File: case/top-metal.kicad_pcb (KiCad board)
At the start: 2 copper layers, 137.8 x 95.7 mm, 26 parts, among them SW1 SW_PUSH, SW10 SW_PUSH, SW11 SW_PUSH, SW12 SW_PUSH, SW13 SW_PUSH, SW14 SW_PUSH, SW15 SW_PUSH, SW16 SW_PUSH, SW17 SW_PUSH, SW18 SW_PUSH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

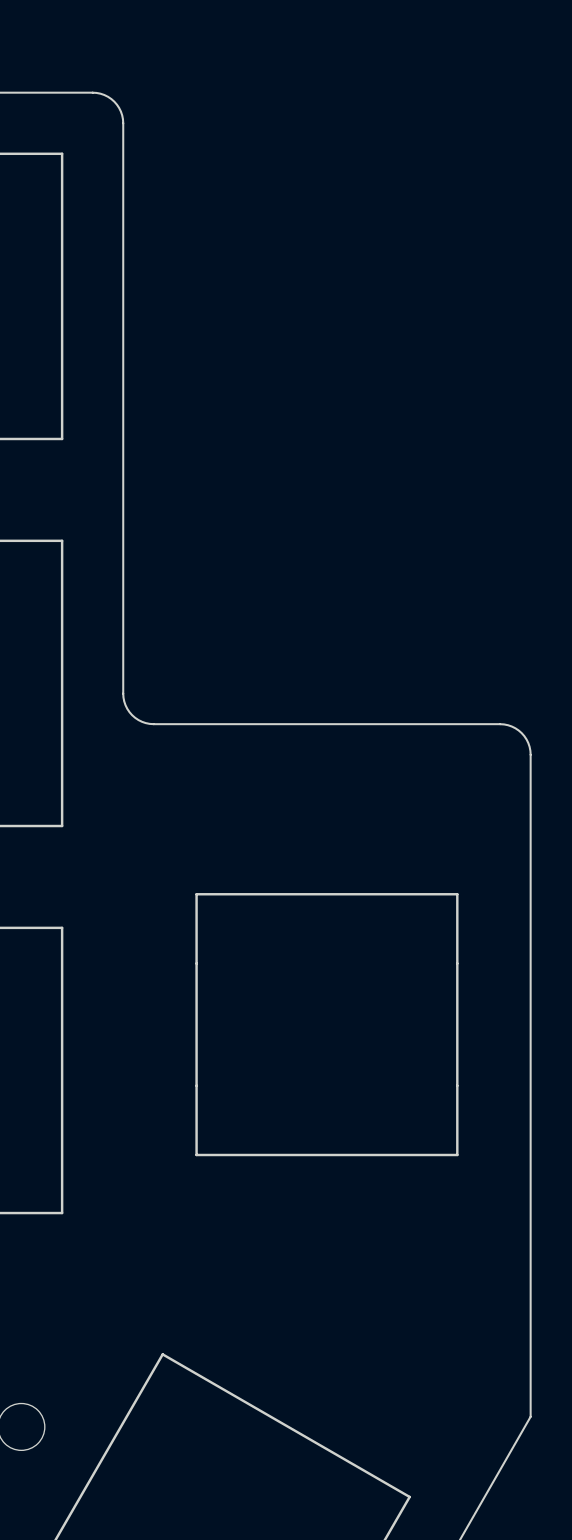
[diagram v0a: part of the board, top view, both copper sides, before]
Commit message: adjust top plate, add new cover in PCB style
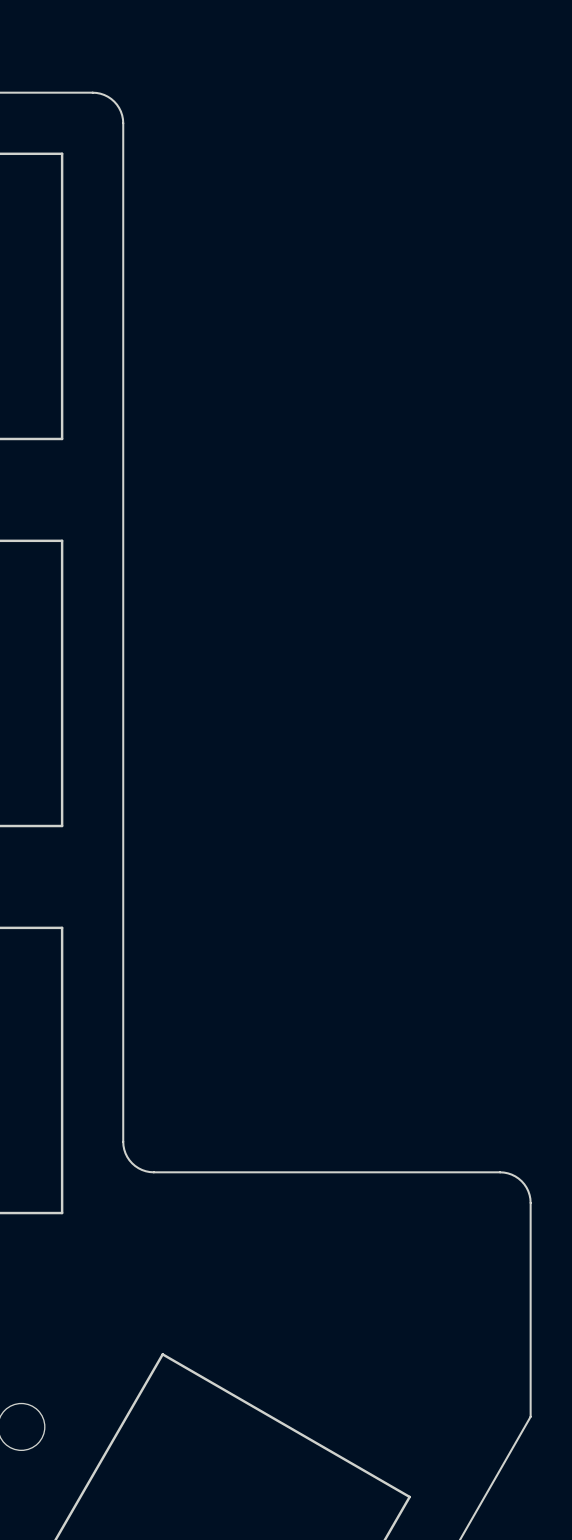
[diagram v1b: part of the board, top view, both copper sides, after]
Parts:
- removed RE1: RotaryEncoder_Switch, pica:EC11_Hole
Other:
- outline, holes or cut-outs redrawn
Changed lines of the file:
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@@
     (fp_line (start 9.525 -9.525) (end -9.525 -9.525) (layer "F.Fab") (width 0.15))
-  )
-  (footprint "pica:EC11_Hole" (layer "F.Cu")
-    (at 188.5 96.75)
-    (property "Sheetfile" "full.kicad_sch")
-    (property "Sheetname" "")
-    (attr through_hole)
-    (fp_text reference "RE1" (at 0 7.7 unlocked) (layer "F.SilkS") hide
-      (effects (font (size 1 1) (thickness 0.15)))
-    )
-    (fp_text value "RotaryEncoder_Switch" (at 0 -7.3 unlocked) (layer "F.Fab") hide
-      (effects (font (size 1 1) (thickness 0.15)))
-    )
-    (fp_line (start 6.4 6.4) (end -6.4 6.4) (layer "Edge.Cuts") (width 0.12))
-    (fp_line (start -6.4 -6.4) (end -6.4 -3) (layer "Edge.Cuts") (width 0.12))
-    (fp_line (start 6.4 -3) (end 6.4 3) (layer "Edge.Cuts") (width 0.12))
-    (fp_line (start 6.4 -3) (end 6.4 -6.4) (layer "Edge.Cuts") (width 0.12))
-    (fp_line (start -6.4 -6.4) (end 6.4 -6.4) (layer "Edge.Cuts") (width 0.12))
-    (fp_line (start -6.4 -3) (end -6.4 3) (layer "Edge.Cuts") (width 0.12))
-    (fp_line (start 6.4 6.4) (end 6.4 3) (layer "Edge.Cuts") (width 0.12))
-    (fp_line (start -6.4 3) (end -6.4 6.4) (layer "Edge.Cuts") (width 0.12))
   )
   (footprint "kbd:SW_Hole" (layer "F.Cu")
@@
   )
   (gr_line (start 103 48.5) (end 119 48.5) (layer "Edge.Cuts") (width 0.1))
-  (gr_line (start 180 82) (end 197 82) (layer "Edge.Cuts") (width 0.1))
+  (gr_arc (start 180 104) (mid 178.93934 103.56066) (end 178.5 102.5) (layer "Edge.Cuts") (width 0.1))
+  (gr_line (start 180 104) (end 197 104) (layer "Edge.Cuts") (width 0.1))
   (gr_arc (start 142 49) (mid 140.93934 48.56066) (end 140.5 47.5) (layer "Edge.Cuts") (width 0.1))
   (gr_arc (start 185.049038 139.450962) (mid 184.138233 140.149868) (end 183 140) (layer "Edge.Cuts") (width 0.1))
@@
   (gr_line (start 183 140) (end 167.5 131) (layer "Edge.Cuts") (width 0.1))
   (gr_arc (start 177 51) (mid 178.06066 51.43934) (end 178.5 52.5) (layer "Edge.Cuts") (width 0.1))
-  (gr_line (start 178.5 52.5) (end 178.5 80.5) (layer "Edge.Cuts") (width 0.1))
+  (gr_line (start 178.5 52.5) (end 178.5 102.5) (layer "Edge.Cuts") (width 0.1))
   (gr_line (start 149 126) (end 167.5 131) (layer "Edge.Cuts") (width 0.1))
-  (gr_arc (start 197 82) (mid 198.060645 82.439345) (end 198.5 83.5) (layer "Edge.Cuts") (width 0.1))
   (gr_line (start 99.925797 59.400232) (end 79.863558 61.099769) (layer "Edge.Cuts") (width 0.1))
   (gr_arc (start 158 49) (mid 158.901388 49.272918) (end 159.5 50) (layer "Edge.Cuts") (width 0.1))
   (gr_line (start 101.5 50) (end 101.5 57.75) (layer "Edge.Cuts") (width 0.1))
+  (gr_arc (start 197 104) (mid 198.06066 104.43934) (end 198.5 105.5) (layer "Edge.Cuts") (width 0.1))
   (gr_arc (start 65.5 115.445189) (mid 64.40507 115.099984) (end 63.874978 114.081632) (layer "Edge.Cuts") (width 0.1))
   (gr_arc (start 84.7 119.1) (mid 83.75732 118.711348) (end 83.3 117.8) (layer "Edge.Cuts") (width 0.1))
@@
   (gr_line (start 84.7 119.1) (end 103 117.5) (layer "Edge.Cuts") (width 0.1))
   (gr_line (start 60.654775 77.9) (end 63.874978 114.081632) (layer "Edge.Cuts") (width 0.1))
+  (gr_line (start 198.5 105.5) (end 198.5 116) (layer "Edge.Cuts") (width 0.1))
   (gr_line (start 78.006854 74.799377) (end 62.018333 76.274974) (layer "Edge.Cuts") (width 0.1))
   (gr_arc (start 81.5 114) (mid 82.594914 114.345225) (end 83.125026 115.363557) (layer "Edge.Cuts") (width 0.1))
-  (gr_arc (start 180 82) (mid 178.93934 81.56066) (end 178.5 80.5) (layer "Edge.Cuts") (width 0.1))
   (gr_line (start 161 51) (end 177 51) (layer "Edge.Cuts") (width 0.1))
   (gr_line (start 103 117.5) (end 130 126) (layer "Edge.Cuts") (width 0.1))
   (gr_arc (start 120.5 47) (mid 120.06066 48.06066) (end 119 48.5) (layer "Edge.Cuts") (width 0.1))
   (gr_line (start 120.5 46) (end 120.5 47) (layer "Edge.Cuts") (width 0.1))
-  (gr_line (start 198.5 83.5) (end 198.5 116) (layer "Edge.Cuts") (width 0.1))
 )

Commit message: fix dxf files
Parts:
- H1, H2, H3, H4, H5: footprint kbd:thread_m2 -> pica:thread_m2_hole
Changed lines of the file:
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@@
     (pad_to_mask_clearance 0)
     (pcbplotparams
-      (layerselection 0x0000080_7ffffffe)
+      (layerselection 0x0001000_7ffffffe)
       (disableapertmacros false)
       (usegerberextensions false)
@@
       (svguseinch false)
       (svgprecision 6)
-      (excludeedgelayer false)
+      (excludeedgelayer true)
       (plotframeref false)
       (viasonmask false)
@@
       (hpglpenspeed 20)
       (hpglpendiameter 15.000000)
-      (dxfpolygonmode true)
+      (dxfpolygonmode false)
       (dxfimperialunits false)
       (dxfusepcbnewfont true)
@@
     (fp_line (start 9.525 9.525) (end 9.525 -9.525) (layer "F.Fab") (width 0.15))
   )
-  (footprint "kbd:thread_m2" (layer "F.Cu")
+  (footprint "pica:thread_m2_hole" (layer "F.Cu")
     (at 160 70.5)
     (descr "Mounting Hole 2.2mm, no annular, M2")
@@
       (effects (font (size 1 1) (thickness 0.15)))
     )
-    (pad "" np_thru_hole circle locked (at 0 0) (size 2.3 2.3) (drill 2.3) (layers *.Cu *.Mask))
-  )
-  (footprint "kbd:thread_m2" (layer "F.Cu")
+    (fp_circle (center 0 0) (end 1.15 0) (layer "Edge.Cuts") (width 0.1) (fill none))
+  )
+  (footprint "pica:thread_m2_hole" (layer "F.Cu")
     (at 100.8 68)
     (descr "Mounting Hole 2.2mm, no annular, M2")
@@
       (effects (font (size 1 1) (thickness 0.15)))
     )
-    (pad "" np_thru_hole circle locked (at 0 0) (size 2.3 2.3) (drill 2.3) (layers *.Cu *.Mask))
+    (fp_circle (center 0 0) (end 1.15 0) (layer "Edge.Cuts") (width 0.1) (fill none))
   )
   (footprint "kbd:SW_Hole" (layer "F.Cu")
@@
     (fp_line (start -9.525 9.525) (end 9.525 9.525) (layer "F.Fab") (width 0.15))
   )
-  (footprint "kbd:thread_m2" (layer "F.Cu")
+  (footprint "pica:thread_m2_hole" (layer "F.Cu")
     (at 122 102.5)
     (descr "Mounting Hole 2.2mm, no annular, M2")
@@
       (effects (font (size 1 1) (thickness 0.15)))
     )
-    (pad "" np_thru_hole circle locked (at 0 0) (size 2.3 2.3) (drill 2.3) (layers *.Cu *.Mask))
+    (fp_circle (center 0 0) (end 1.15 0) (layer "Edge.Cuts") (width 0.1) (fill none))
   )
   (footprint "kbd:SW_Hole" (layer "F.Cu")
@@
     (fp_line (start 9.525 9.525) (end 9.525 -9.525) (layer "F.Fab") (width 0.15))
   )
-  (footprint "kbd:thread_m2" (layer "F.Cu")
+  (footprint "pica:thread_m2_hole" (layer "F.Cu")
     (at 81.25 94.25 5)
     (descr "Mounting Hole 2.2mm, no annular, M2")
@@
       (effects (font (size 1 1) (thickness 0.15)))
     )
-    (pad "" np_thru_hole circle locked (at 0 0 5) (size 2.3 2.3) (drill 2.3) (layers *.Cu *.Mask))
+    (fp_circle (center 0 0) (end 1.15 0) (layer "Edge.Cuts") (width 0.1) (fill none))
   )
   (footprint "kbd:SW_Hole" (layer "F.Cu")
@@
     (fp_line (start -9.525 9.525) (end 9.525 9.525) (layer "F.Fab") (width 0.15))
   )
-  (footprint "kbd:thread_m2" (layer "F.Cu")
+  (footprint "pica:thread_m2_hole" (layer "F.Cu")
     (at 173.5 116.5)
     (descr "Mounting Hole 2.2mm, no annular, M2")
@@
       (effects (font (size 1 1) (thickness 0.15)))
     )
-    (pad "" np_thru_hole circle locked (at 0 0) (size 2.3 2.3) (drill 2.3) (layers *.Cu *.Mask))
-  )
-  (footprint "kbd:SW_Hole" (layer "F.Cu")
+    (fp_circle (center 0 0) (end 1.15 0) (layer "Edge.Cuts") (width 0.1) (fill none))
+  )
+  (footprint "kbd:SW_Hole" (layer "F.Cu")
